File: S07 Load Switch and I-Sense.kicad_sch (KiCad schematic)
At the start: 59 parts, among them Q20 DMN65D8LFB-7, Q21 DMN65D8LFB-7, Q22 DMN65D8LFB-7, U10 TLV9002IDSG, U6 TPS22811, U7 TPS22811, U8 TLV9002IDSG, U9 TPS22811

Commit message: Use KiCad standard footprints for chip resistors and capacitors
The imported Lattech R/C footprints have poor land patterns (the 0402s
use 0.635 mm circular pads) and cause tombstoning in assembly. Replace
all 139 chip resistors and capacitors with KiCad's standard IPC-7351
nominal footprints:

  Res 0402/0603/1206/2512 -> Resistor_SMD:R_xxxx_xxxxMetric (87)
  Cap 0402/0603/0805/1206/1210 -> Capacitor_SMD:C_xxxx_xxxxMetric (52)

Each part keeps its position, rotation, side, pad nets, schematic link
and reference/value text placement. The pads are on the same axis with
pad 1 on the same side, and every old pad centre lies inside the new
pad, so existing tracks still connect. Zones are refilled.

Schematic Footprint fields and the symbols' footprint filters point at
the new footprints, and the unused imported R/C footprints are removed
from the project library. Electrolytic capacitors are not changed.

DRC: 0 unconnected items, as before. Tracks, vias, zone outlines and
all other footprints are unchanged. 11 courtyard overlaps are new,
because the old footprints had no courtyards.

Co-Authored-By: Claude Opus 5.5 <noreply@anthropic.com>
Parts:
- C44, C45, C48, C49, C50, C54, C56: footprint EVO2513-0_5_0-import-fps:Cap 0603 H0-9 -> Capacitor_SMD:C_0603_1608Metric
- C46, C47, C51, C52, C53: footprint EVO2513-0_5_0-import-fps:Cap 0402 H0-6 R -> Capacitor_SMD:C_0402_1005Metric
- R49, R50, R51, R52, R53, R54, R55, R56, R57, R58, R59, R60, R61, R62, R63, R64, R65, R66, R67, R68, R69, R70, R71, R72, R73, R74, R75, R76, R77, R78, R79, R80, R81: footprint EVO2513-0_5_0-import-fps:Res 0402 H0-45 R -> Resistor_SMD:R_0402_1005Metric
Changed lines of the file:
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@@
 			)
 		)
-		(property "Footprint" "EVO2513-0_5_0-import-fps:Cap 0402 H0-6 R"
+		(property "Footprint" "Capacitor_SMD:C_0402_1005Metric"
 			(at 254 83.6422 0)
 			(hide yes)
@@
 			)
 		)
-		(property "Footprint" "EVO2513-0_5_0-import-fps:Res 0402 H0-45 R"
+		(property "Footprint" "Resistor_SMD:R_0402_1005Metric"
 			(at 102.87 143.3322 0)
 			(hide yes)
@@
 			)
 		)
-		(property "Footprint" "EVO2513-0_5_0-import-fps:Res 0402 H0-45 R"
+		(property "Footprint" "Resistor_SMD:R_0402_1005Metric"
 			(at 76.2 84.9122 0)
 			(hide yes)
@@
 			)
 		)
-		(property "Footprint" "EVO2513-0_5_0-import-fps:Res 0402 H0-45 R"
+		(property "Footprint" "Resistor_SMD:R_0402_1005Metric"
 			(at 236.22 83.6422 0)
 			(hide yes)
@@
 			)
 		)
-		(property "Footprint" "EVO2513-0_5_0-import-fps:Cap 0603 H0-9"
+		(property "Footprint" "Capacitor_SMD:C_0603_1608Metric"
 			(at 57.15 84.9122 0)
 			(hide yes)
@@
 			)
 		)
-		(property "Footprint" "EVO2513-0_5_0-import-fps:Res 0402 H0-45 R"
+		(property "Footprint" "Resistor_SMD:R_0402_1005Metric"
 			(at 73.66 211.9122 0)
 			(hide yes)
@@
 			)
 		)
-		(property "Footprint" "EVO2513-0_5_0-import-fps:Res 0402 H0-45 R"
+		(property "Footprint" "Resistor_SMD:R_0402_1005Metric"
 			(at 118.11 262.7122 0)
 			(hide yes)
@@
 			)
 		)
-		(property "Footprint" "EVO2513-0_5_0-import-fps:Res 0402 H0-45 R"
+		(property "Footprint" "Resistor_SMD:R_0402_1005Metric"
 			(at 146.05 247.4722 0)
 			(hide yes)
@@
 			)
 		)
-		(property "Footprint" "EVO2513-0_5_0-import-fps:Cap 0603 H0-9"
+		(property "Footprint" "Capacitor_SMD:C_0603_1608Metric"
 			(at 54.61 211.9122 0)
 			(hide yes)
@@
 			)
 		)
-		(property "Footprint" "EVO2513-0_5_0-import-fps:Res 0402 H0-45 R"
+		(property "Footprint" "Resistor_SMD:R_0402_1005Metric"
 			(at 93.98 143.3322 0)
 			(hide yes)
@@
 			)
 		)
-		(property "Footprint" "EVO2513-0_5_0-import-fps:Cap 0603 H0-9"
+		(property "Footprint" "Capacitor_SMD:C_0603_1608Metric"
 			(at 226.06 83.6422 0)
 			(hide yes)
@@
 			)
 		)
-		(property "Footprint" "EVO2513-0_5_0-import-fps:Res 0402 H0-45 R"
+		(property "Footprint" "Resistor_SMD:R_0402_1005Metric"
 			(at 320.04 175.0822 0)
 			(hide yes)
@@
 			)
 		)
-		(property "Footprint" "EVO2513-0_5_0-import-fps:Res 0402 H0-45 R"
+		(property "Footprint" "Resistor_SMD:R_0402_1005Metric"
 			(at 271.78 142.0622 0)
 			(hide yes)
@@
 			)
 		)
-		(property "Footprint" "EVO2513-0_5_0-import-fps:Res 0402 H0-45 R"
+		(property "Footprint" "Resistor_SMD:R_0402_1005Metric"
 			(at 292.1 190.3222 0)
 			(hide yes)
@@
 			)
 		)
-		(property "Footprint" "EVO2513-0_5_0-import-fps:Res 0402 H0-45 R"
+		(property "Footprint" "Resistor_SMD:R_0402_1005Metric"
 			(at 148.59 120.4722 0)
 			(hide yes)
@@
 			)
 		)
-		(property "Footprint" "EVO2513-0_5_0-import-fps:Res 0402 H0-45 R"
+		(property "Footprint" "Resistor_SMD:R_0402_1005Metric"
 			(at 245.11 83.6422 0)
 			(hide yes)
@@
 			)
 		)
-		(property "Footprint" "EVO2513-0_5_0-import-fps:Res 0402 H0-45 R"
+		(property "Footprint" "Resistor_SMD:R_0402_1005Metric"
 			(at 130.81 53.1622 0)
 			(hide yes)
@@
 			)
 		)
-		(property "Footprint" "EVO2513-0_5_0-import-fps:Res 0402 H0-45 R"
+		(property "Footprint" "Resistor_SMD:R_0402_1005Metric"
 			(at 142.24 190.3222 0)
 			(hide yes)
@@
 			)
 		)
-		(property "Footprint" "EVO2513-0_5_0-import-fps:Cap 0603 H0-9"
+		(property "Footprint" "Capacitor_SMD:C_0603_1608Metric"
 			(at 172.72 54.4322 0)
 			(hide yes)
@@
 			)
 		)
-		(property "Footprint" "EVO2513-0_5_0-import-fps:Res 0402 H0-45 R"
+		(property "Footprint" "Resistor_SMD:R_0402_1005Metric"
 			(at 325.12 62.0522 0)
 			(hide yes)
@@
 			)
 		)
-		(property "Footprint" "EVO2513-0_5_0-import-fps:Cap 0402 H0-6 R"
+		(property "Footprint" "Capacitor_SMD:C_0402_1005Metric"
 			(at 278.13 234.7722 0)
 			(hide yes)
@@
 			)
 		)
-		(property "Footprint" "EVO2513-0_5_0-import-fps:Res 0402 H0-45 R"
+		(property "Footprint" "Resistor_SMD:R_0402_1005Metric"
 			(at 317.5 119.2022 0)
 			(hide yes)
@@
 			)
 		)
-		(property "Footprint" "EVO2513-0_5_0-import-fps:Res 0402 H0-45 R"
+		(property "Footprint" "Resistor_SMD:R_0402_1005Metric"
 			(at 299.72 62.0522 0)
 			(hide yes)
@@
 			)
 		)
-		(property "Footprint" "EVO2513-0_5_0-import-fps:Res 0402 H0-45 R"
+		(property "Footprint" "Resistor_SMD:R_0402_1005Metric"
 			(at 100.33 270.3322 0)
 			(hide yes)
@@
 			)
 		)
-		(property "Footprint" "EVO2513-0_5_0-import-fps:Cap 0603 H0-9"
+		(property "Footprint" "Capacitor_SMD:C_0603_1608Metric"
 			(at 355.6 234.7722 0)
 			(hide yes)
@@
 			)
 		)
-		(property "Footprint" "EVO2513-0_5_0-import-fps:Res 0402 H0-45 R"
+		(property "Footprint" "Resistor_SMD:R_0402_1005Metric"
 			(at 262.89 142.0622 0)
 			(hide yes)
@@
 			)
 		)
-		(property "Footprint" "EVO2513-0_5_0-import-fps:Res 0402 H0-45 R"
+		(property "Footprint" "Resistor_SMD:R_0402_1005Metric"
 			(at 64.77 211.9122 0)
 			(hide yes)
@@
 			)
 		)
-		(property "Footprint" "EVO2513-0_5_0-import-fps:Res 0402 H0-45 R"
+		(property "Footprint" "Resistor_SMD:R_0402_1005Metric"
 			(at 156.21 63.3222 0)
 			(hide yes)
@@
 			)
 		)
-		(property "Footprint" "EVO2513-0_5_0-import-fps:Res 0402 H0-45 R"
+		(property "Footprint" "Resistor_SMD:R_0402_1005Metric"
 			(at 144.78 63.3222 0)
 			(hide yes)
@@
 			)
 		)
-		(property "Footprint" "EVO2513-0_5_0-import-fps:Cap 0603 H0-9"
+		(property "Footprint" "Capacitor_SMD:C_0603_1608Metric"
 			(at 170.18 181.4322 0)
 			(hide yes)
@@
 			)
 		)
-		(property "Footprint" "EVO2513-0_5_0-import-fps:Res 0402 H0-45 R"
+		(property "Footprint" "Resistor_SMD:R_0402_1005Metric"
 			(at 289.56 134.4422 0)
 			(hide yes)
@@
 			)
 		)
-		(property "Footprint" "EVO2513-0_5_0-import-fps:Res 0402 H0-45 R"
+		(property "Footprint" "Resistor_SMD:R_0402_1005Metric"
 			(at 128.27 180.1622 0)
 			(hide yes)
@@
 			)
 		)
-		(property "Footprint" "EVO2513-0_5_0-import-fps:Res 0402 H0-45 R"
+		(property "Footprint" "Resistor_SMD:R_0402_1005Metric"
 			(at 67.31 84.9122 0)
 			(hide yes)
@@
 			)
 		)
-		(property "Footprint" "EVO2513-0_5_0-import-fps:Res 0402 H0-45 R"
+		(property "Footprint" "Resistor_SMD:R_0402_1005Metric"
 			(at 128.27 190.3222 0)
 			(hide yes)
@@
 			)
 		)
-		(property "Footprint" "EVO2513-0_5_0-import-fps:Res 0402 H0-45 R"
+		(property "Footprint" "Resistor_SMD:R_0402_1005Metric"
 			(at 130.81 63.3222 0)
 			(hide yes)
@@
 			)
 		)
-		(property "Footprint" "EVO2513-0_5_0-import-fps:Cap 0402 H0-6 R"
+		(property "Footprint" "Capacitor_SMD:C_0402_1005Metric"
 			(at 326.39 234.7722 0)
 			(hide yes)
@@
 			)
 		)
-		(property "Footprint" "EVO2513-0_5_0-import-fps:Cap 0402 H0-6 R"
+		(property "Footprint" "Capacitor_SMD:C_0402_1005Metric"
 			(at 85.09 84.9122 0)
 			(hide yes)
@@
 			)
 		)
-		(property "Footprint" "EVO2513-0_5_0-import-fps:Res 0402 H0-45 R"
+		(property "Footprint" "Resistor_SMD:R_0402_1005Metric"
 			(at 120.65 135.7122 0)
 			(hide yes)
@@
 			)
 		)
-		(property "Footprint" "EVO2513-0_5_0-import-fps:Res 0402 H0-45 R"
+		(property "Footprint" "Resistor_SMD:R_0402_1005Metric"
 			(at 274.32 197.9422 0)
 			(hide yes)
@@
 			)
 		)
-		(property "Footprint" "EVO2513-0_5_0-import-fps:Res 0402 H0-45 R"
+		(property "Footprint" "Resistor_SMD:R_0402_1005Metric"
 			(at 91.44 270.3322 0)
 			(hide yes)
@@
 			)
 		)
-		(property "Footprint" "EVO2513-0_5_0-import-fps:Cap 0603 H0-9"
+		(property "Footprint" "Capacitor_SMD:C_0603_1608Metric"
 			(at 341.63 53.1622 0)
 			(hide yes)
@@
 			)
 		)
-		(property "Footprint" "EVO2513-0_5_0-import-fps:Cap 0402 H0-6 R"
+		(property "Footprint" "Capacitor_SMD:C_0402_1005Metric"
 			(at 82.55 211.9122 0)
 			(hide yes)
@@
 			)
 		)
-		(property "Footprint" "EVO2513-0_5_0-import-fps:Res 0402 H0-45 R"
+		(property "Footprint" "Resistor_SMD:R_0402_1005Metric"
 			(at 299.72 51.8922 0)
 			(hide yes)
@@
 			)
 		)
-		(property "Footprint" "EVO2513-0_5_0-import-fps:Res 0402 H0-45 R"
+		(property "Footprint" "Resistor_SMD:R_0402_1005Metric"
 			(at 313.69 62.0522 0)
 			(hide yes)
@@
 			)
 		)
-		(property "Footprint" "EVO2513-0_5_0-import-fps:Res 0402 H0-45 R"
+		(property "Footprint" "Resistor_SMD:R_0402_1005Metric"
 			(at 153.67 190.3222 0)
 			(hide yes)

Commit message: Fix schematic ERC issues from the import
ERC across all seven sheets reported 1481 issues from the import:

- Every item sat 43 mil off KiCad's 50 mil connection grid in Y, so new
  wires would not snap to existing pins. Each sheet's contents are
  shifted 7 mil (0.1778 mm) onto the grid; the library symbol
  definitions are untouched and a uniform shift keeps every connection.
  A few wire corners on S06 were off grid on their own (at 6740 mil,
  7620 mil and y 3290 mil); they move to the nearest grid point, which
  removes two 10 mil stubs and moves #PWR065 with its wire.
- Nine wires ran 1.27-2.54 mm past the label sitting on them (ID on S01;
  LDVR1/2 and HDVR1/2 on S06), leaving dangling ends. They are trimmed
  back to the label.
- GND, +12V, +3V3MCU and +5V enter through connector pins, so ERC had
  no power source for them. A PWR_FLAG (#FLG01-#FLG04) sits on each.
- The title-block module name used the Altium formula
  ${COPY(DOCUMENTNAME,5,LENGTH(DOCUMENTNAME)-11)}, which KiCad cannot
  evaluate. Each sheet now carries the title it produced.

ERC: 1481 -> 0. The netlist still matches the PCB's 147 nets.

Update PCB from Schematic was rerun afterwards. It changes metadata only:
footprint filters, unit and pin-function data from the symbols, and the
KiLib_Generator fields dropped from the 139 standard R/C footprints. No
placement or copper changes.

Co-Authored-By: Claude Opus 5.5 <noreply@anthropic.com>
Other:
- note added: "Load Switch and I-Sense"
- note removed: "${COPY(DOCUMENTNAME,5,LENGTH(DOCUMENTNAME)-11)}"

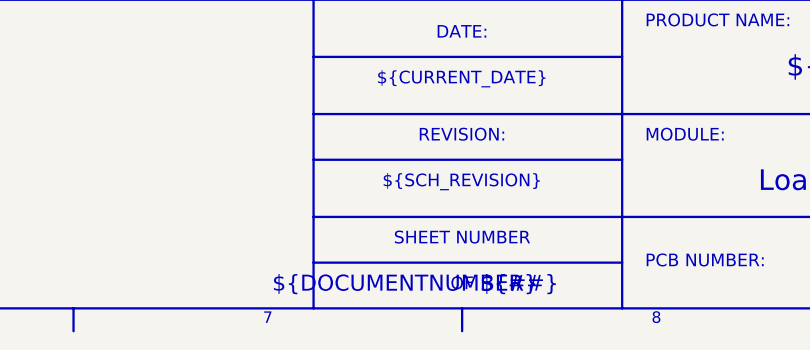
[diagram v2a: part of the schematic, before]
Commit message: Convert the schematic to a hierarchical root sheet
The Altium import produced seven KiCad 10 top-level sheets, with S01's
content in EVO2513-0_5_0.kicad_sch. kicad-cli only loads the first of
those, so command-line ERC, netlist and DRC parity checks saw S01 alone.

- EVO2513-0_5_0.kicad_sch is now a root sheet holding one sheet symbol per
  sheet; S01's content moves to "S01 External Connectors.kicad_sch".
- Each sheet symbol keeps its old top-level sheet UUID, so symbol
  references, net names and connectivity are unchanged: the netlist from
  the new root is identical to the previous whole-design netlist (229
  components, 147 nets). Cross-sheet nets still use global labels.
- The board's 229 footprint paths take the hierarchical form
  /<sheet>/<symbol>, and S01's footprints point at the new sheet file.
  No copper or placement changes.
- Every title block read "sheet 7 of 7" (a single DOCUMENTNUMBER project
  variable). Sheet numbers now use the page number: the root is page 1
  and S01-S07 are pages 2-8.

kicad-cli ERC over the whole design: 0 errors, 0 warnings. DRC with
schematic parity: 0 parity issues, 450 violations as before.

Co-Authored-By: Claude Opus 5.5 <noreply@anthropic.com>
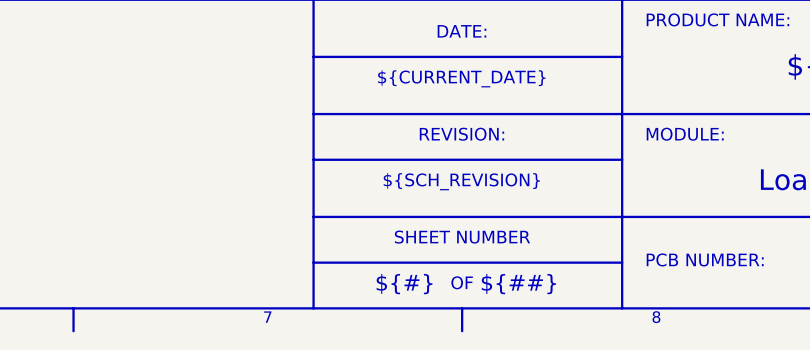
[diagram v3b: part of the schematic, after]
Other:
- note added: "${#}"
- note removed: "${DOCUMENTNUMBER}"

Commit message: Link the sheets through hierarchical labels and sheet pins
The 78 cross-sheet global labels on S01-S07 become hierarchical labels,
and each sheet symbol on the root gets a pin per label name (71 pins).
On the root, each pin connects through a short wire to a global label
with the net name. Global labels there, rather than local ones, keep the
35 net names free of a "/" sheet-path prefix, so the net classes and the
board's nets are unchanged.

Layout: S01 External Connectors on the left with its pins on the right
edge; S02-S04 and S05-S07 in two columns with their pins on the left.

The netlist is identical to before (229 components, 147 nets, same names
and pins). kicad-cli ERC: 0 errors, 0 warnings. DRC with schematic
parity: 0 parity issues, 450 violations as before.

Co-Authored-By: Claude Opus 5.5 <noreply@anthropic.com>
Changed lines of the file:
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@@
 		)
 	)
-	(global_label "OUTSBC"
+	(hierarchical_label "OUTSBC"
 		(shape passive)
 		(at 194.31 46.99 0)
-		(fields_autoplaced yes)
 		(effects
 			(font
@@
 			(justify left)
 		)
-		(property "Intersheetrefs" "${INTERSHEET_REFS}"
-			(at 194.31 46.99 0)
-			(effects
-				(font
-					(size 1.27 1.27)
-				)
-				(justify left)
-				(hide yes)
-			)
-		)
 	)
-	(global_label "OUTEXT"
+	(hierarchical_label "OUTEXT"
 		(shape passive)
 		(at 363.22 45.72 0)
-		(fields_autoplaced yes)
 		(effects
 			(font
@@
 			(justify left)
 		)
-		(property "Intersheetrefs" "${INTERSHEET_REFS}"
-			(at 363.22 45.72 0)
-			(effects
-				(font
-					(size 1.27 1.27)
-				)
-				(justify left)
-				(hide yes)
-			)
-		)
 	)
-	(global_label "IAMPEXT"
+	(hierarchical_label "IAMPEXT"
 		(shape passive)
 		(at 356.87 119.38 0)
-		(fields_autoplaced yes)
 		(effects
 			(font
@@
 			(justify left)
 		)
-		(property "Intersheetrefs" "${INTERSHEET_REFS}"
-			(at 356.87 119.38 0)
-			(effects
-				(font
-					(size 1.27 1.27)
-				)
-				(justify left)
-				(hide yes)
-			)
-		)
 	)
-	(global_label "IAMPDAQ"
+	(hierarchical_label "IAMPDAQ"
 		(shape passive)
 		(at 185.42 247.65 0)
-		(fields_autoplaced yes)
 		(effects
 			(font
@@
 			(justify left)
 		)
-		(property "Intersheetrefs" "${INTERSHEET_REFS}"
-			(at 185.42 247.65 0)
-			(effects
-				(font
-					(size 1.27 1.27)
-				)
-				(justify left)
-				(hide yes)
-			)
-		)
 	)
-	(global_label "IAMPSBC"
+	(hierarchical_label "IAMPSBC"
 		(shape passive)
 		(at 187.96 120.65 0)
-		(fields_autoplaced yes)
 		(effects
 			(font
@@
 			(justify left)
 		)
-		(property "Intersheetrefs" "${INTERSHEET_REFS}"
-			(at 187.96 120.65 0)
-			(effects
-				(font
-					(size 1.27 1.27)
-				)
-				(justify left)
-				(hide yes)
-			)
-		)
 	)
-	(global_label "ENDAQ"
+	(hierarchical_label "ENDAQ"
 		(shape passive)
 		(at 38.1 185.42 180)
-		(fields_autoplaced yes)
 		(effects
 			(font
@@
 			(justify right)
 		)
-		(property "Intersheetrefs" "${INTERSHEET_REFS}"
-			(at 38.1 185.42 0)
-			(effects
-				(font
-					(size 1.27 1.27)
-				)
-				(justify right)
-				(hide yes)
-			)
-		)
 	)
-	(global_label "OUTDAQ"
+	(hierarchical_label "OUTDAQ"
 		(shape passive)
 		(at 194.31 173.99 0)
-		(fields_autoplaced yes)
 		(effects
 			(font
@@
 			(justify left)
 		)
-		(property "Intersheetrefs" "${INTERSHEET_REFS}"
-			(at 194.31 173.99 0)
-			(effects
-				(font
-					(size 1.27 1.27)
-				)
-				(justify left)
-				(hide yes)
-			)
-		)
 	)
-	(global_label "IAMPREG"
+	(hierarchical_label "IAMPREG"
 		(shape passive)
 		(at 342.9 175.26 0)
-		(fields_autoplaced yes)
 		(effects
 			(font
@@
 			(justify left)
 		)
-		(property "Intersheetrefs" "${INTERSHEET_REFS}"
-			(at 342.9 175.26 0)
-			(effects
-				(font
-					(size 1.27 1.27)
-				)
-				(justify left)
-				(hide yes)
-			)
-		)
 	)
-	(global_label "ENEXT"
+	(hierarchical_label "ENEXT"
 		(shape passive)
 		(at 209.55 57.15 180)
-		(fields_autoplaced yes)
 		(effects
 			(font
@@
 			(justify right)
 		)
-		(property "Intersheetrefs" "${INTERSHEET_REFS}"
-			(at 209.55 57.15 0)
-			(effects
-				(font
-					(size 1.27 1.27)
-				)
-				(justify right)
-				(hide yes)
-			)
-		)
 	)
-	(global_label "ENSBC"
+	(hierarchical_label "ENSBC"
 		(shape passive)
 		(at 40.64 58.42 180)
-		(fields_autoplaced yes)
 		(effects
 			(font
@@
 			(justify right)
 		)
-		(property "Intersheetrefs" "${INTERSHEET_REFS}"
-			(at 40.64 58.42 0)
-			(effects
-				(font
-					(size 1.27 1.27)
-				)
-				(justify right)
-				(hide yes)
-			)
-		)
 	)
-	(global_label "CDC"
+	(hierarchical_label "CDC"
 		(shape passive)
 		(at 251.46 175.26 180)
-		(fields_autoplaced yes)
 		(effects
 			(font
@@
 			(justify right)
 		)
-		(property "Intersheetrefs" "${INTERSHEET_REFS}"
-			(at 251.46 175.26 0)
-			(effects
-				(font
-					(size 1.27 1.27)
-				)
-				(justify right)
-				(hide yes)
-			)
-		)
 	)
